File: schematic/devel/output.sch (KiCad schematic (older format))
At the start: 5 parts, among them J2 CONN_X1, J3 CONN_X2, J4 CONN_Y1, J5 CONN_Y2, J6 CONN_PWR

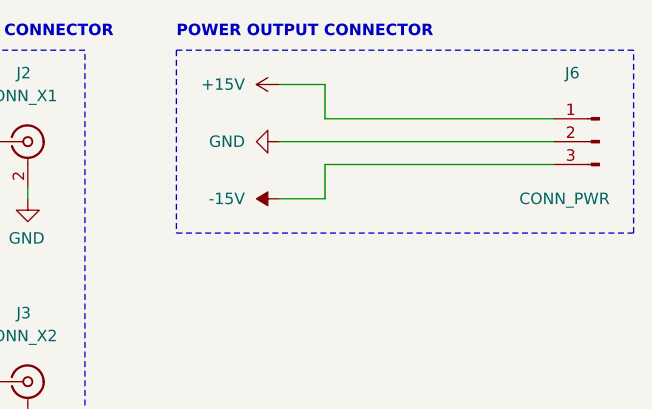
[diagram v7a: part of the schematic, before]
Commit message: merged circuit sheets to single sheet, removed extra diodes, changed diode type
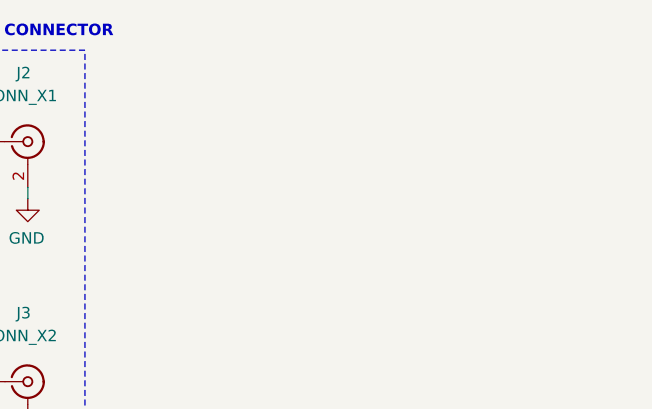
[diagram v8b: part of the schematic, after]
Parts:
- removed J6: CONN_PWR, Connector_PinHeader_1.00mm:PinHeader_1x03_P1.00mm_Vertical, symbol Connector:Conn_01x03_Male
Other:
- note removed: "POWER OUTPUT CONNECTOR"
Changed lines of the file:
@@
 Text GLabel 1350 1900 0    50   Input ~ 10
 -X1
-Wire Notes Line
-	4400 2300 4400 1500
-Text Notes 2400 1450 0    50   ~ 10
-POWER OUTPUT CONNECTOR
-Wire Notes Line
-	2400 1500 2400 2300
-Wire Notes Line
-	4400 1500 2400 1500
-$Comp
-L power:+15V #PWR0126
-U 1 1 5C9CB573
-P 2850 1650
-F 0 "#PWR0126" H 2850 1500 50  0001 C CNN
-F 1 "+15V" V 2850 1800 50  0000 L CNN
-F 2 "" H 2850 1650 50  0001 C CNN
-F 3 "" H 2850 1650 50  0001 C CNN
-	1    2850 1650
-	0    -1   -1   0
-$EndComp
-$Comp
-L power:-15V #PWR0127
-U 1 1 5C9CD644
-P 2850 2150
-F 0 "#PWR0127" H 2850 2250 50  0001 C CNN
-F 1 "-15V" V 2850 2300 50  0000 L CNN
-F 2 "" H 2850 2150 50  0001 C CNN
-F 3 "" H 2850 2150 50  0001 C CNN
-	1    2850 2150
-	0    -1   -1   0
-$EndComp
-$Comp
-L power:GND #PWR0128
-U 1 1 5C9CE4B3
-P 2850 1900
-F 0 "#PWR0128" H 2850 1650 50  0001 C CNN
-F 1 "GND" V 2850 1750 50  0000 R CNN
-F 2 "" H 2850 1900 50  0001 C CNN
-F 3 "" H 2850 1900 50  0001 C CNN
-	1    2850 1900
-	0    1    1    0
-$EndComp
-$Comp
-L Connector:Conn_01x03_Male J6
-U 1 1 5C9D0AD0
-P 4250 1900
-F 0 "J6" H 4400 2200 50  0000 R CNN
-F 1 "CONN_PWR" H 4600 1650 50  0000 R CNN
-F 2 "Connector_PinHeader_1.00mm:PinHeader_1x03_P1.00mm_Vertical" H 4250 1900 50  0001 C CNN
-F 3 "~" H 4250 1900 50  0001 C CNN
-	1    4250 1900
-	-1   0    0    -1
-$EndComp
-Wire Wire Line
-	4050 1800 3050 1800
-Wire Wire Line
-	3050 1800 3050 1650
-Wire Wire Line
-	3050 1650 2850 1650
-Wire Wire Line
-	2850 1900 4050 1900
-Wire Wire Line
-	4050 2000 3050 2000
-Wire Wire Line
-	3050 2000 3050 2150
-Wire Wire Line
-	3050 2150 2850 2150
-Wire Notes Line
-	2400 2300 4400 2300
 Wire Wire Line
 	1350 1900 1550 1900
